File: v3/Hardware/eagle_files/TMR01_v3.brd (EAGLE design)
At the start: 28.4 x 28.4 mm, 28 parts, among them IC1 DS3231/SO, U1 ATMEGA328P_TQFP

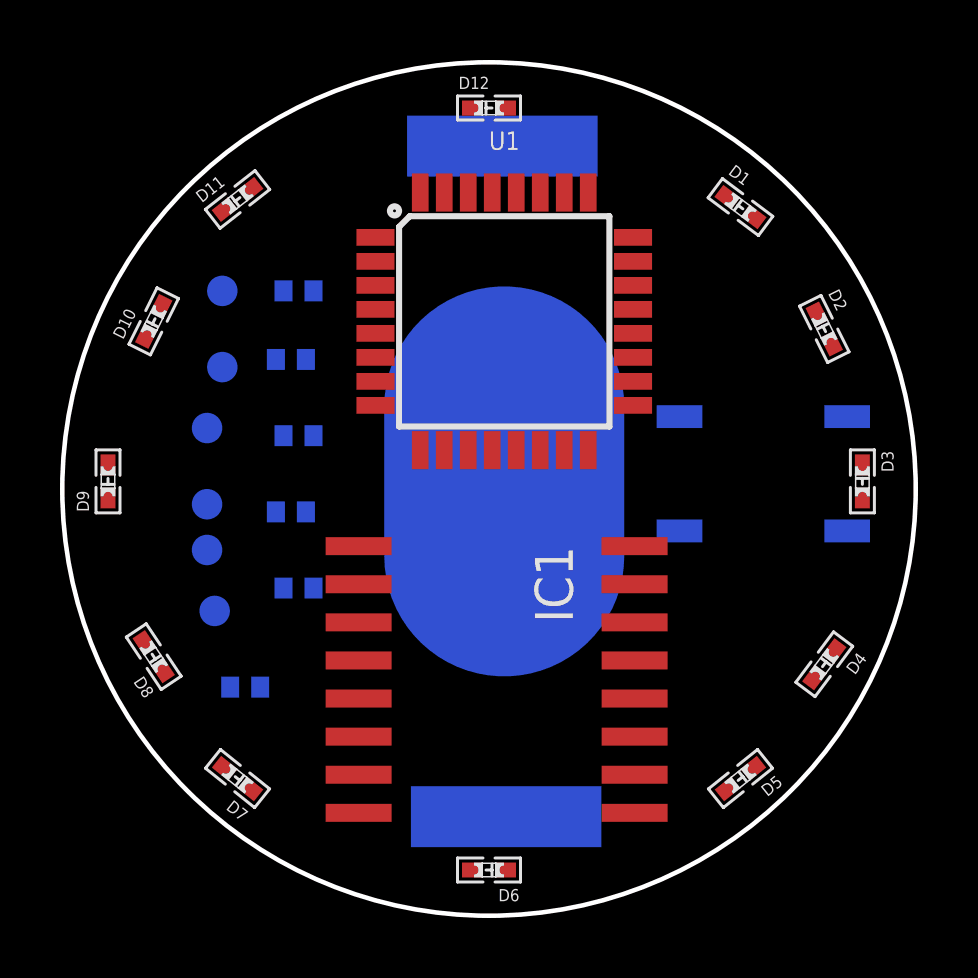
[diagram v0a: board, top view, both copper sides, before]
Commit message: fixed sda scl in rtc
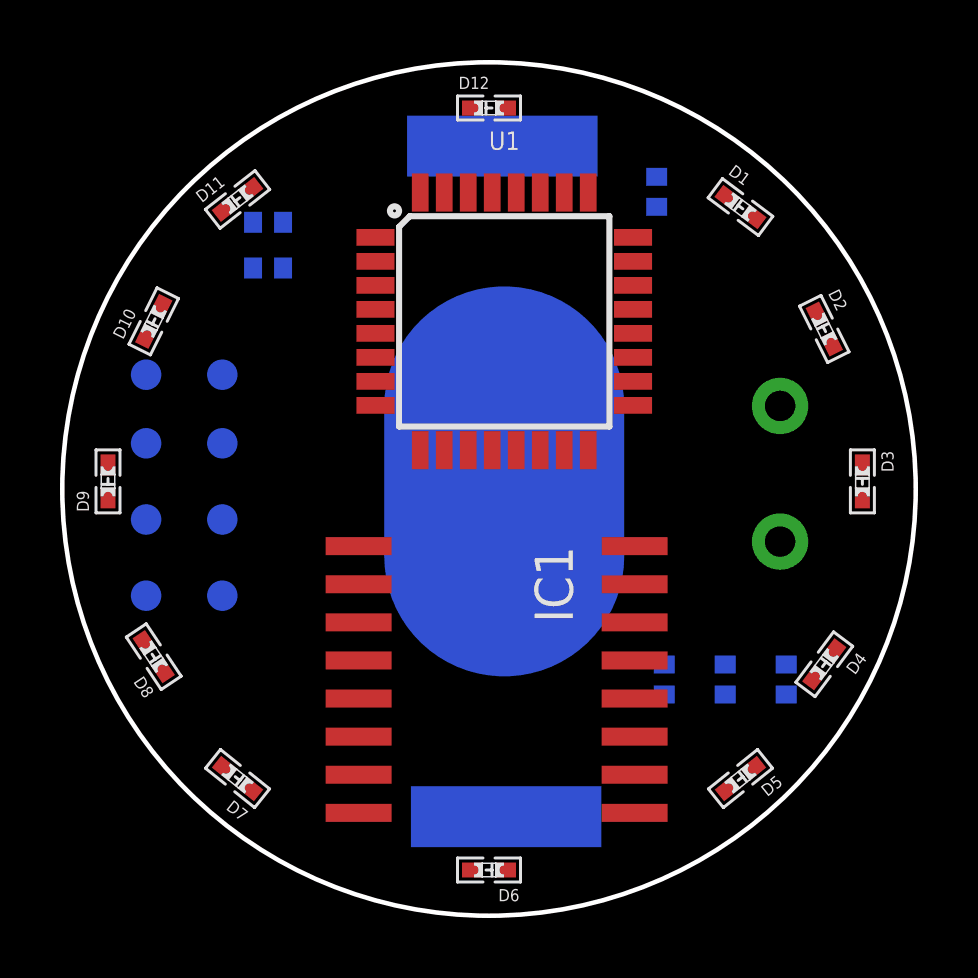
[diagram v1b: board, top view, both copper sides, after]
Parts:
- added TP3, TP4: TEST-POINT3X4, SparkFun-Connectors:PAD.03X.04
- S1: value MOMENTARY-SWITCH-SPST-SMD-5.2MM -> MOMENTARY-SWITCH-SPST; device SparkFun-Switches:TACTILE_SWITCH_SMD_5.2MM -> SparkFun-Switches:TACTILE_SWITCH_PTH_2_AHE
- moved C1 21.5 mm to (19.8, 24.1), turned to 270 degrees
- moved R1 20.8 mm to (24.1, 7.87), turned to 270 degrees
- moved R2 18.0 mm to (22.1, 7.87), turned to 270 degrees
- moved R3 14.7 mm to (20.1, 7.87), turned to 270 degrees
- moved R5 12.2 mm to (6.86, 23.1), turned to 180 degrees
- moved R4 8.16 mm to (6.86, 21.6), turned to 180 degrees
- moved TP9 8.03 mm to (2.79, 13.2)
- moved TP8 7.62 mm to (5.33, 10.7)
- moved TP12 3.59 mm to (5.33, 15.7)
- moved TP10 3.09 mm to (5.33, 13.2)
- moved TP11 2.87 mm to (2.79, 15.7)
- moved TP7 2.34 mm to (2.79, 10.7), turned to 180 degrees
- moved S1 1.02 mm to (24.4, 14.7), turned to 180 degrees
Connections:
- net PUSH: now also S1.2; no longer S1.3
- net RX: now also TP3.P$1
- net SCL: now also IC1.16, R2.1; no longer IC1.15, R3.1
- net SDA: now also IC1.15, R3.1; no longer IC1.16, R2.1
- net TX: now also TP4.P$1

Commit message: pins output modified, not using miso mosi connected to leds
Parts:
- moved R2 8.44 mm to (23.1, 16.3), flipped to the top, turned to 0 degrees
- moved R3 6.82 mm to (23.1, 14.0), flipped to the top, turned to 0 degrees
- moved R1 3.94 mm to (23.1, 11.7), flipped to the top, turned to 0 degrees
- moved S1 2.30 mm to (26.7, 14.5)
- moved R4 0.76 mm to (6.86, 20.8)
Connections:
- removed net PUSH: R5.2, S1.2, U1.32
- new net D4: D4.P$1, U1.23
- new net D5: D5.P$1, U1.13
- net D1: now also U1.26; no longer U1.25
- net D12: now also U1.32; no longer U1.26
- net D2: now also U1.25; no longer U1.24
- net D3: now also U1.24; no longer U1.23
- net D6: now also U1.12; no longer U1.13
- net MISO: no longer D5.P$1
- net SCK: no longer D4.P$1
- net SS: now also R5.2, S1.2
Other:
- board text added: "GND"
- board text added: "MISO"
- board text added: "MOSI"
- board text added: "RST"
- board text added: "RX"
- board text added: "SCK"
- board text added: "TX"
- board text added: "VCC"

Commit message: gerbers generated
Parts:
- moved TP7 23.7 mm to (26.4, 13.0)
- moved TP9 23.7 mm to (26.4, 15.0)
- moved TP10 21.2 mm to (26.4, 10.9)
- moved S1 5.48 mm to (25.4, 19.8), turned to 150.9 degrees
- moved TP12 4.58 mm to (2.79, 11.9)
- moved TP3 4.37 mm to (2.79, 14.5)
- moved TP11 3.30 mm to (2.79, 19.1)
- moved TP8 2.84 mm to (2.79, 9.40)
- moved TP4 1.27 mm to (2.79, 16.8)
- moved D2 0.25 mm to (25.1, 19.6)
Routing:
- net VCC: track 0.00 -> 107.7 mm, vias 0 -> 2
- net GND: track 0.00 -> 90.6 mm, vias 0 -> 4
- net N$3: track 0.00 -> 89.5 mm
- net SDA: track 0.00 -> 35.4 mm, vias 0 -> 2
- net SS: track 0.00 -> 27.7 mm, vias 0 -> 1
- net SCL: track 0.00 -> 25.3 mm, vias 0 -> 2
- net D6: track 0.00 -> 23.6 mm
- net RST: track 0.00 -> 18.3 mm, vias 0 -> 1
- net D5: track 0.00 -> 16.3 mm, vias 0 -> 2
- net MOSI: track 0.00 -> 16.2 mm, vias 0 -> 1
- net D7: track 0.00 -> 16.1 mm
- net D4: track 0.00 -> 16.0 mm
- net RX: track 0.00 -> 15.5 mm, vias 0 -> 1
- net TX: track 0.00 -> 13.5 mm, vias 0 -> 1
- net D8: track 0.00 -> 12.9 mm
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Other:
- board text added: "1"
- board text added: "10"
- board text added: "11"
- board text added: "2"
- board text added: "3"
- board text added: "4"
- board text added: "5"
- board text added: "7"
- board text added: "8"
- board text added: "9"
- board text added: "AHERRERO"
- board text added: "Bora"
- board text added: "Watch"

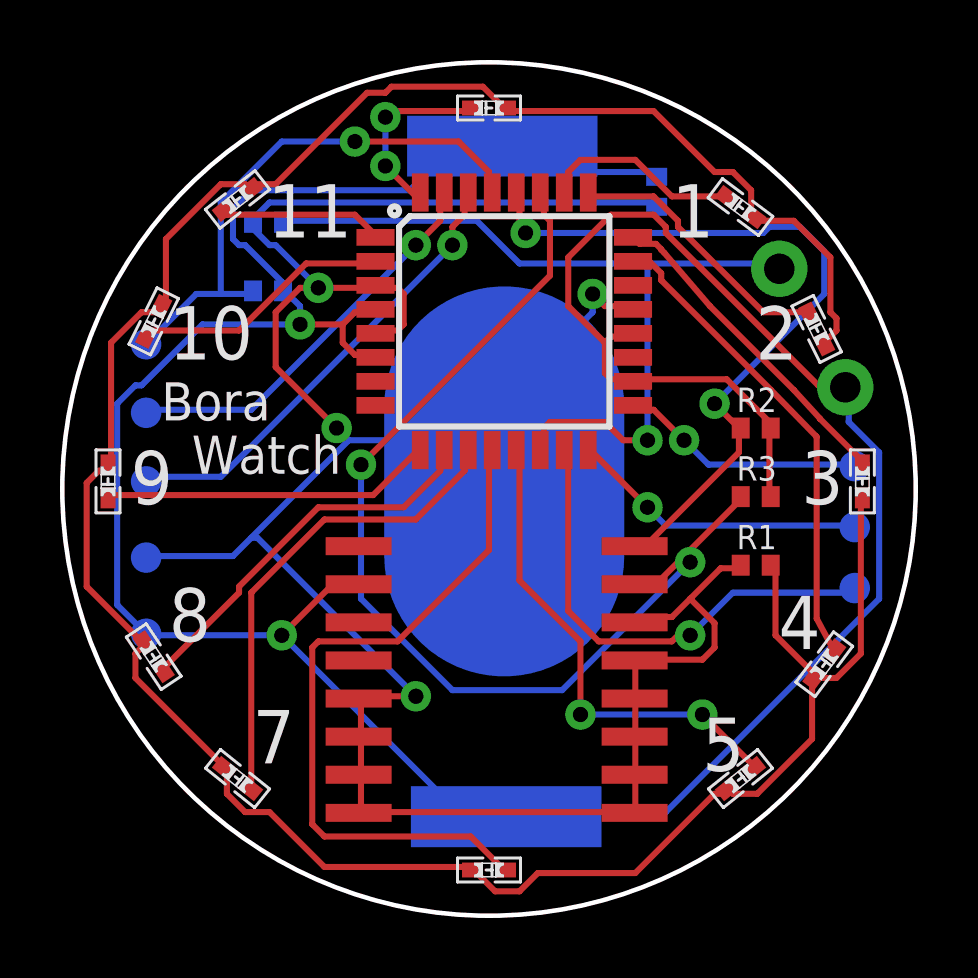
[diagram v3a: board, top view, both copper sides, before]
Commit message: 0402 leds possible wrong footprint. Changed temporaly by resistors footprint
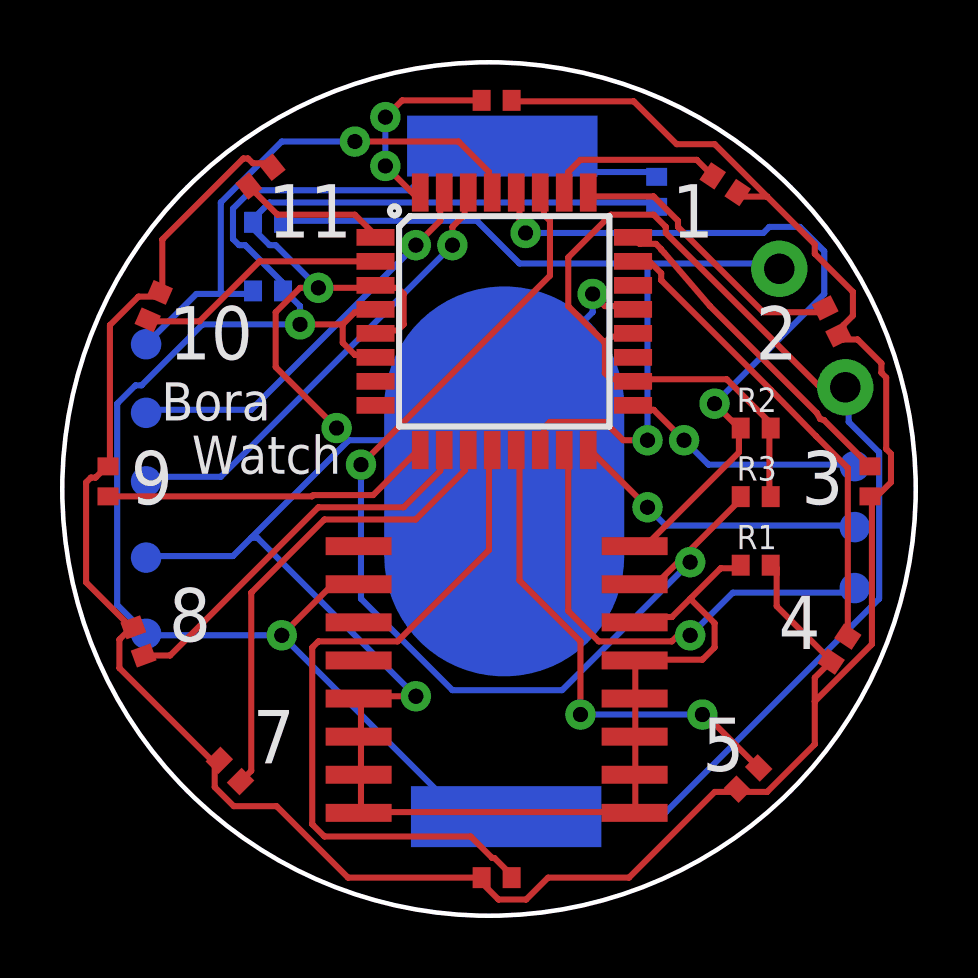
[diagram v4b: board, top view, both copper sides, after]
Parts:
- D1, D10, D11, D12, D2, D3, D4, D5, D6, D7, D8, D9: device standardparts:0402.LED -> Perfect_0402:0402
- moved D11 1.08 mm to (6.60, 24.6), turned to 38.7 degrees
- moved D1 0.92 mm to (22.1, 24.4), turned to 326.3 degrees
- moved D4 0.72 mm to (25.9, 8.89), turned to 236.3 degrees
- moved D8 0.72 mm to (2.54, 9.14), turned to 110.2 degrees
- moved D2 0.57 mm to (25.7, 19.8)
- moved D10 0.51 mm to (3.05, 20.3), turned to 66.3 degrees
- moved D12 0.36 mm to (14.5, 27.2)
- moved D6 0.36 mm to (14.5, 1.27)
- moved D7 0.36 mm to (5.59, 4.83), turned to 135 degrees
- moved D3 0.25 mm to (26.9, 14.5)
- moved D5 0.25 mm to (22.9, 4.57), turned to 225 degrees
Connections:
- net D1: now also D1.1; no longer D1.P$1
- net D10: now also D10.1; no longer D10.P$1
- net D11: now also D11.1; no longer D11.P$1
- net D12: now also D12.1; no longer D12.P$1
- net D2: now also D2.1; no longer D2.P$1
- net D3: now also D3.1; no longer D3.P$1
- net D4: now also D4.1; no longer D4.P$1
- net D5: now also D5.1; no longer D5.P$1
- net D6: now also D6.1; no longer D6.P$1
- net D7: now also D7.1; no longer D7.P$1
- net D8: now also D8.1; no longer D8.P$1
- net D9: now also D9.1; no longer D9.P$1
- net N$3: now also D1.2, D10.2, D11.2, D12.2, D2.2, D3.2, D4.2, D5.2, D6.2, D7.2, D8.2, D9.2; no longer D1.P$2, D10.P$2, D11.P$2, D12.P$2, D2.P$2, D3.P$2, D4.P$2, D5.P$2, D6.P$2, D7.P$2, D8.P$2, D9.P$2
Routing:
- net D1: track 6.75 -> 5.97 mm
- net D2: track 9.15 -> 9.72 mm
- net D11: track 5.48 -> 4.96 mm
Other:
- board text added: "v3.1"

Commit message: recover status with leds
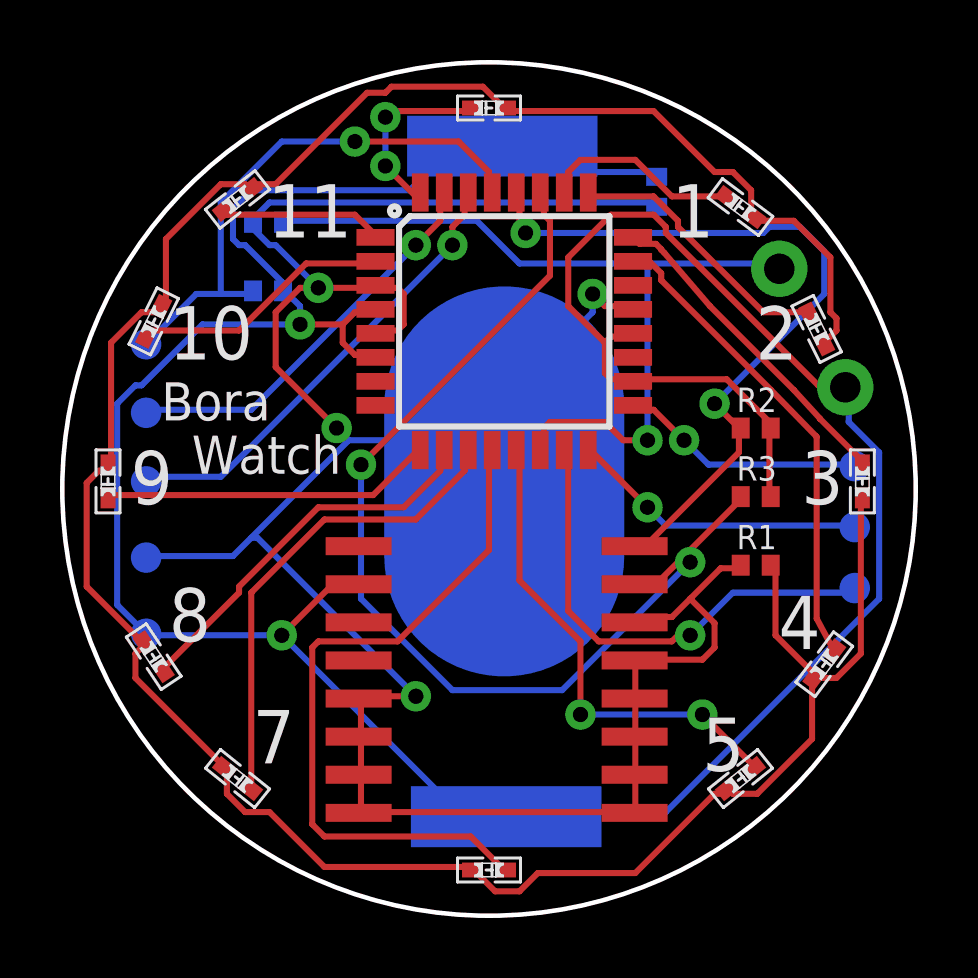
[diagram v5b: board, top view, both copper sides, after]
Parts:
- D1, D10, D11, D12, D2, D3, D4, D5, D6, D7, D8, D9: device Perfect_0402:0402 -> standardparts:0402.LED
- moved D11 1.08 mm to (5.84, 23.9), turned to 38 degrees
- moved D1 0.92 mm to (22.6, 23.6), turned to 323.2 degrees
- moved D4 0.72 mm to (25.4, 8.38), turned to 233.2 degrees
- moved D8 0.72 mm to (3.05, 8.64), turned to 123.7 degrees
- moved D2 0.57 mm to (25.1, 19.6)
- moved D10 0.51 mm to (3.05, 19.8), turned to 63.5 degrees
- moved D12 0.36 mm to (14.2, 26.9)
- moved D6 0.36 mm to (14.2, 1.52)
- moved D7 0.36 mm to (5.84, 4.57), turned to 141.3 degrees
- moved D3 0.25 mm to (26.7, 14.5)
- moved D5 0.25 mm to (22.6, 4.57), turned to 218.7 degrees
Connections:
- net D1: now also D1.P$1; no longer D1.1
- net D10: now also D10.P$1; no longer D10.1
- net D11: now also D11.P$1; no longer D11.1
- net D12: now also D12.P$1; no longer D12.1
- net D2: now also D2.P$1; no longer D2.1
- net D3: now also D3.P$1; no longer D3.1
- net D4: now also D4.P$1; no longer D4.1
- net D5: now also D5.P$1; no longer D5.1
- net D6: now also D6.P$1; no longer D6.1
- net D7: now also D7.P$1; no longer D7.1
- net D8: now also D8.P$1; no longer D8.1
- net D9: now also D9.P$1; no longer D9.1
- net N$3: now also D1.P$2, D10.P$2, D11.P$2, D12.P$2, D2.P$2, D3.P$2, D4.P$2, D5.P$2, D6.P$2, D7.P$2, D8.P$2, D9.P$2; no longer D1.2, D10.2, D11.2, D12.2, D2.2, D3.2, D4.2, D5.2, D6.2, D7.2, D8.2, D9.2
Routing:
- net D1: track 5.97 -> 6.75 mm
- net D2: track 9.72 -> 9.15 mm
- net D11: track 4.96 -> 5.48 mm
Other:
- board text removed: "v3.1"
